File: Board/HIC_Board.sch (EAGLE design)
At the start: 104 parts, among them IC1 CXA2075, IC2 4069UBF, IC3 LM358D, IC4 FMW1A, IC5 FMW1A, IC6 IMN10A, Q1 2SA1037, Q2 2SC2411k

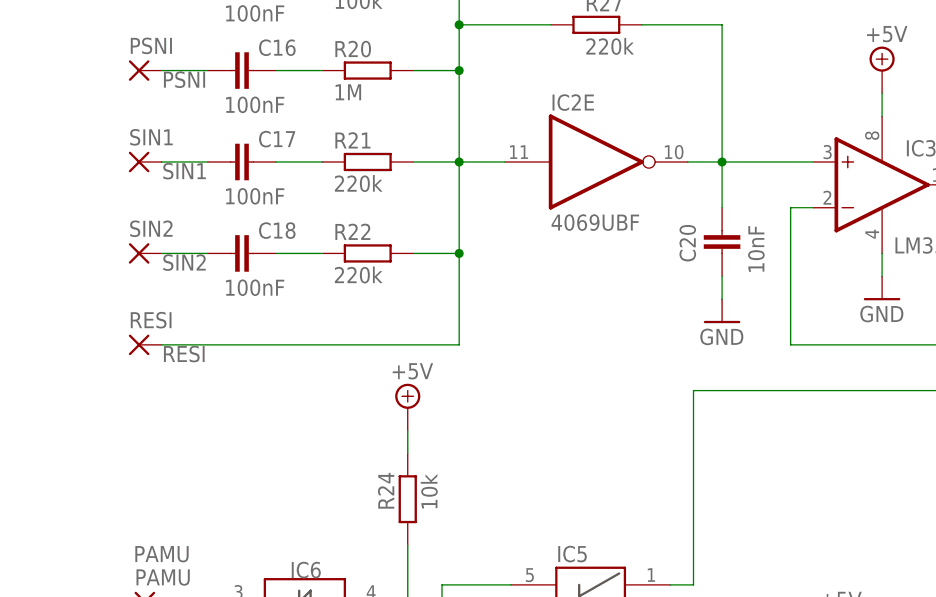
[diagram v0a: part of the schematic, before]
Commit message: Updated 21.09.2023
Updated to v1.2. The error was fixed, the resistor was added for HB-F1XDJ computer (see the readme file)
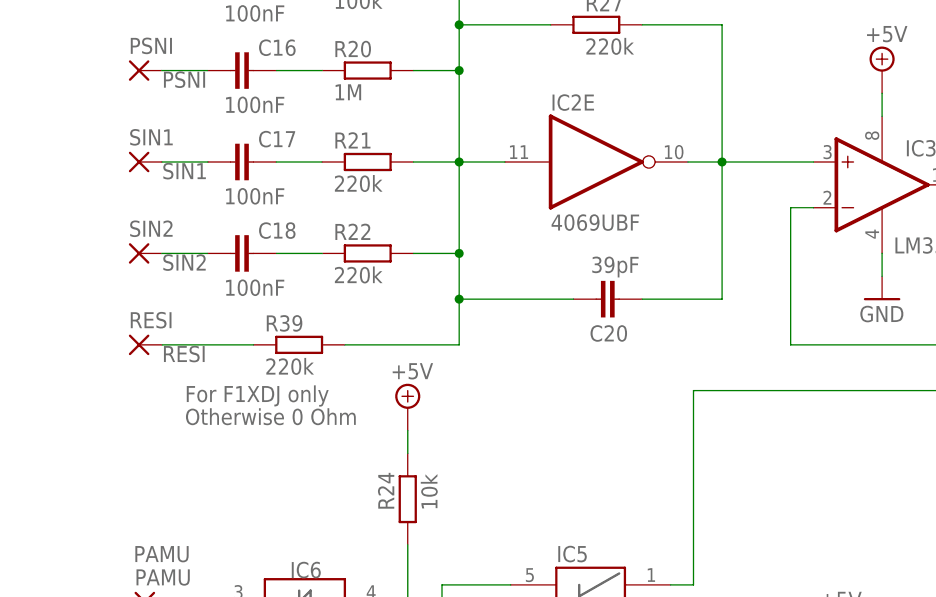
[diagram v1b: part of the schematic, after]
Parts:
- added R39: 220k, rcl:R-EU_R0805
- C20: value 10nF -> 39pF
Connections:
- new net N$12: R39.1, RESI.P
- net GND: no longer C20.2
- net N$43: now also C20.2; no longer C20.1
- net RESI: now also C20.1, R39.2; no longer RESI.P
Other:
- note added: "For F1XDJ only"
- note added: "Otherwise 0 Ohm"
- note added: "Re-engineering and improvements by RBSC (c) 2021-2023"
- note added: "Version 1.2"
- note removed: "Re-engineering and improvements by RBSC (c) 2021"
- note removed: "Version 1.0"
- moved on the sheet: C20
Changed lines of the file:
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@@
 <setting verticaltext="up"/>
 </settings>
-<grid distance="0.1" unitdist="inch" unit="inch" style="lines" multiple="1" display="no" altdistance="0.01" altunitdist="inch" altunit="inch"/>
+<grid distance="0.05" unitdist="inch" unit="inch" style="lines" multiple="1" display="no" altdistance="0.01" altunitdist="inch" altunit="inch"/>
 <layers>
 <layer number="1" name="Top" color="4" fill="1" visible="no" active="no"/>
@@
 <attribute name="OC_FARNELL" value="unknown"/>
 </part>
-<part name="C20" library="rcl" deviceset="C-EU" device="C0805" value="10nF">
+<part name="C20" library="rcl" deviceset="C-EU" device="C0805" value="39pF">
 <attribute name="MF" value=""/>
 <attribute name="MPN" value=""/>
@@
 </part>
 <part name="GND16" library="supply1" deviceset="GND" device=""/>
-<part name="GND17" library="supply1" deviceset="GND" device=""/>
+<part name="R39" library="rcl" deviceset="R-EU_" device="R0805" value="220k">
+<attribute name="MF" value=""/>
+<attribute name="MPN" value=""/>
+<attribute name="OC_FARNELL" value="unknown"/>
+</part>
 </parts>
 <sheets>
@@
 <text x="60.96" y="-75.565" size="1.6764" layer="97" rot="R180">CSYNC</text>
 <text x="1.27" y="-2.54" size="3.81" layer="104">NTSC HIC board for Sony/Panasonic MSX2/MSX2+ computers</text>
-<text x="1.27" y="-7.62" size="3.556" layer="104">Re-engineering and improvements by RBSC (c) 2021</text>
-<text x="1.27" y="-12.7" size="3.556" layer="104">Version 1.0</text>
+<text x="1.27" y="-7.62" size="3.556" layer="104">Re-engineering and improvements by RBSC (c) 2021-2023</text>
+<text x="1.27" y="-12.7" size="3.556" layer="104">Version 1.2</text>
 <text x="48.26" y="-65.405" size="1.6764" layer="97">SC</text>
 <text x="94.488" y="-46.863" size="1.6764" layer="97">R</text>
@@
 <text x="5.588" y="-146.558" size="1.6764" layer="97">CSI</text>
 <text x="266.7" y="-157.48" size="1.778" layer="95">Optional</text>
+<text x="144.78" y="-66.04" size="1.778" layer="95">For F1XDJ only</text>
+<text x="144.78" y="-68.58" size="1.778" layer="95">Otherwise 0 Ohm</text>
 </plain>
 <instances>
@@
 <attribute name="VALUE" x="189.23" y="-27.432" size="1.778" layer="96"/>
 </instance>
-<instance part="C20" gate="G$1" x="204.47" y="-46.99" smashed="yes">
-<attribute name="OC_FARNELL" x="204.47" y="-46.99" size="1.778" layer="96" rot="R270" display="off"/>
-<attribute name="MF" x="204.47" y="-46.99" size="1.778" layer="96" rot="R270" display="off"/>
-<attribute name="MPN" x="204.47" y="-46.99" size="1.778" layer="96" rot="R270" display="off"/>
-<attribute name="NAME" x="201.549" y="-50.546" size="1.778" layer="95" rot="R90"/>
-<attribute name="VALUE" x="209.169" y="-51.816" size="1.778" layer="96" rot="R90"/>
+<instance part="C20" gate="G$1" x="190.5" y="-54.61" smashed="yes" rot="R90">
+<attribute name="OC_FARNELL" x="190.5" y="-54.61" size="1.778" layer="96" display="off"/>
+<attribute name="MF" x="190.5" y="-54.61" size="1.778" layer="96" display="off"/>
+<attribute name="MPN" x="190.5" y="-54.61" size="1.778" layer="96" display="off"/>
+<attribute name="NAME" x="194.056" y="-57.531" size="1.778" layer="95" rot="R180"/>
+<attribute name="VALUE" x="195.326" y="-49.911" size="1.778" layer="96" rot="R180"/>
 </instance>
 <instance part="R33" gate="G$1" x="240.03" y="-41.91" smashed="yes">
@@
 </instance>
 <instance part="GND16" gate="1" x="38.735" y="-38.735"/>
-<instance part="GND17" gate="1" x="204.47" y="-57.15"/>
+<instance part="R39" gate="G$1" x="157.48" y="-59.69" smashed="yes">
+<attribute name="OC_FARNELL" x="157.48" y="-59.69" size="1.778" layer="96" rot="R180" display="off"/>
+<attribute name="MF" x="157.48" y="-59.69" size="1.778" layer="96" rot="R180" display="off"/>
+<attribute name="MPN" x="157.48" y="-59.69" size="1.778" layer="96" rot="R180" display="off"/>
+<attribute name="NAME" x="153.67" y="-58.1914" size="1.778" layer="95"/>
+<attribute name="VALUE" x="153.67" y="-62.992" size="1.778" layer="96"/>
+</instance>
 </instances>
 <busses>
@@
 <pinref part="GND16" gate="1" pin="GND"/>
 </segment>
-<segment>
-<pinref part="C20" gate="G$1" pin="2"/>
-<pinref part="GND17" gate="1" pin="GND"/>
-<wire x1="204.47" y1="-54.61" x2="204.47" y2="-52.07" width="0.1524" layer="91"/>
-</segment>
 </net>
 <net name="+5V" class="0">
@@
 <wire x1="170.18" y1="-29.21" x2="175.26" y2="-29.21" width="0.1524" layer="91"/>
 <junction x="175.26" y="-29.21"/>
-<pinref part="RESI" gate="1" pin="P"/>
-<wire x1="142.24" y1="-59.69" x2="175.26" y2="-59.69" width="0.1524" layer="91"/>
 <junction x="175.26" y="-49.53"/>
 <pinref part="IC2" gate="E" pin="I"/>
-<wire x1="175.26" y1="-59.69" x2="175.26" y2="-49.53" width="0.1524" layer="91"/>
+<wire x1="175.26" y1="-59.69" x2="175.26" y2="-54.61" width="0.1524" layer="91"/>
+<wire x1="175.26" y1="-54.61" x2="175.26" y2="-49.53" width="0.1524" layer="91"/>
 <wire x1="175.26" y1="-39.37" x2="180.34" y2="-39.37" width="0.1524" layer="91"/>
 <pinref part="R27" gate="G$1" pin="1"/>
@@
 <junction x="175.26" y="-24.13"/>
 <label x="142.24" y="-61.595" size="1.778" layer="95"/>
+<pinref part="C20" gate="G$1" pin="1"/>
+<wire x1="175.26" y1="-54.61" x2="187.96" y2="-54.61" width="0.1524" layer="91"/>
+<junction x="175.26" y="-54.61"/>
+<pinref part="R39" gate="G$1" pin="2"/>
+<wire x1="162.56" y1="-59.69" x2="175.26" y2="-59.69" width="0.1524" layer="91"/>
 </segment>
 </net>
@@
 <pinref part="IC3" gate="A" pin="+IN"/>
 <wire x1="204.47" y1="-39.37" x2="214.63" y2="-39.37" width="0.1524" layer="91"/>
-<pinref part="C20" gate="G$1" pin="1"/>
-<wire x1="204.47" y1="-44.45" x2="204.47" y2="-39.37" width="0.1524" layer="91"/>
+<pinref part="C20" gate="G$1" pin="2"/>
+<wire x1="195.58" y1="-54.61" x2="204.47" y2="-54.61" width="0.1524" layer="91"/>
+<wire x1="204.47" y1="-54.61" x2="204.47" y2="-39.37" width="0.1524" layer="91"/>
 </segment>
 </net>
@@
 </segment>
 </net>
+<net name="N$12" class="0">
+<segment>
+<pinref part="RESI" gate="1" pin="P"/>
+<pinref part="R39" gate="G$1" pin="1"/>
+<wire x1="142.24" y1="-59.69" x2="152.4" y2="-59.69" width="0.1524" layer="91"/>
+</segment>
+</net>
